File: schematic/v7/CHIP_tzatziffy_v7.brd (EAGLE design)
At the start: 40.9 x 49.8 mm, 56 parts, among them J1 2X20-CHIP0.7_DRILL, Q2 2N7002ET1G, U1 LMR62421, U3 DS2431P, X1 FH12-40S-0.5SH

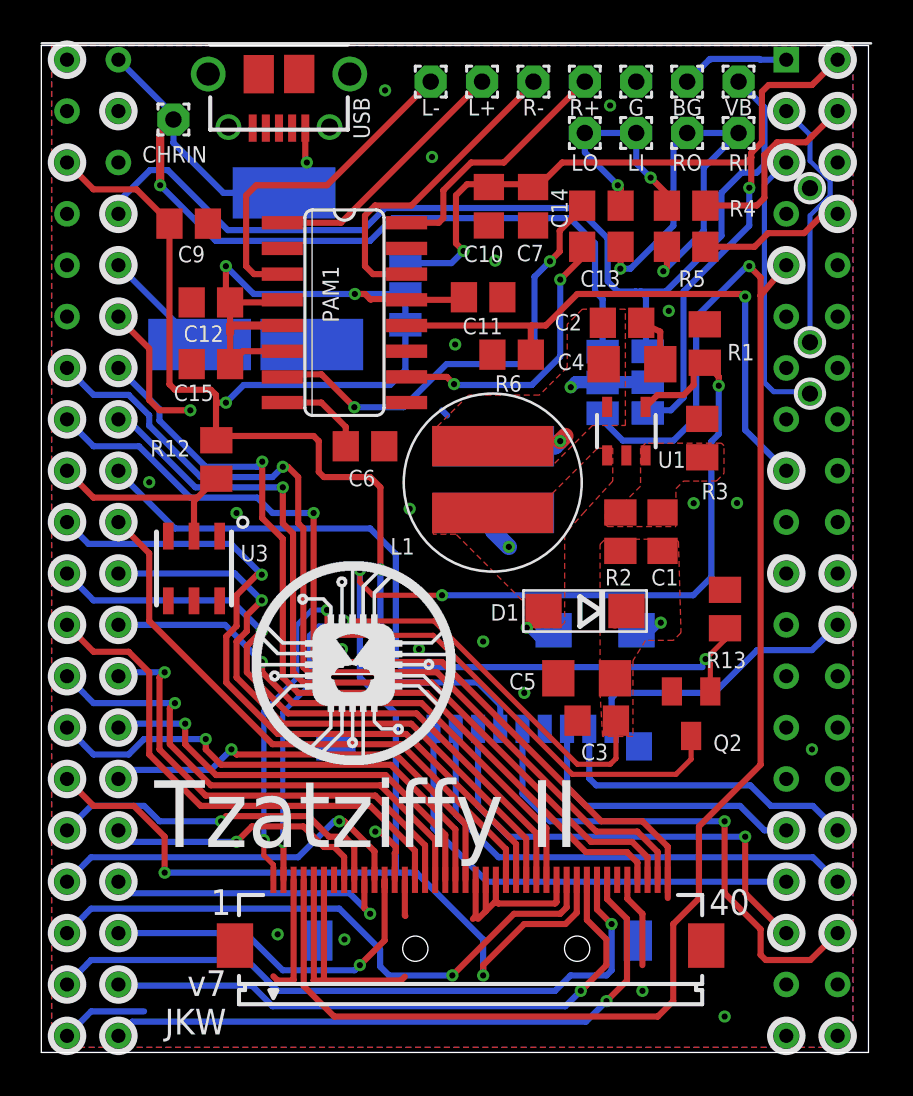
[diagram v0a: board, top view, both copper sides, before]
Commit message: added power supply
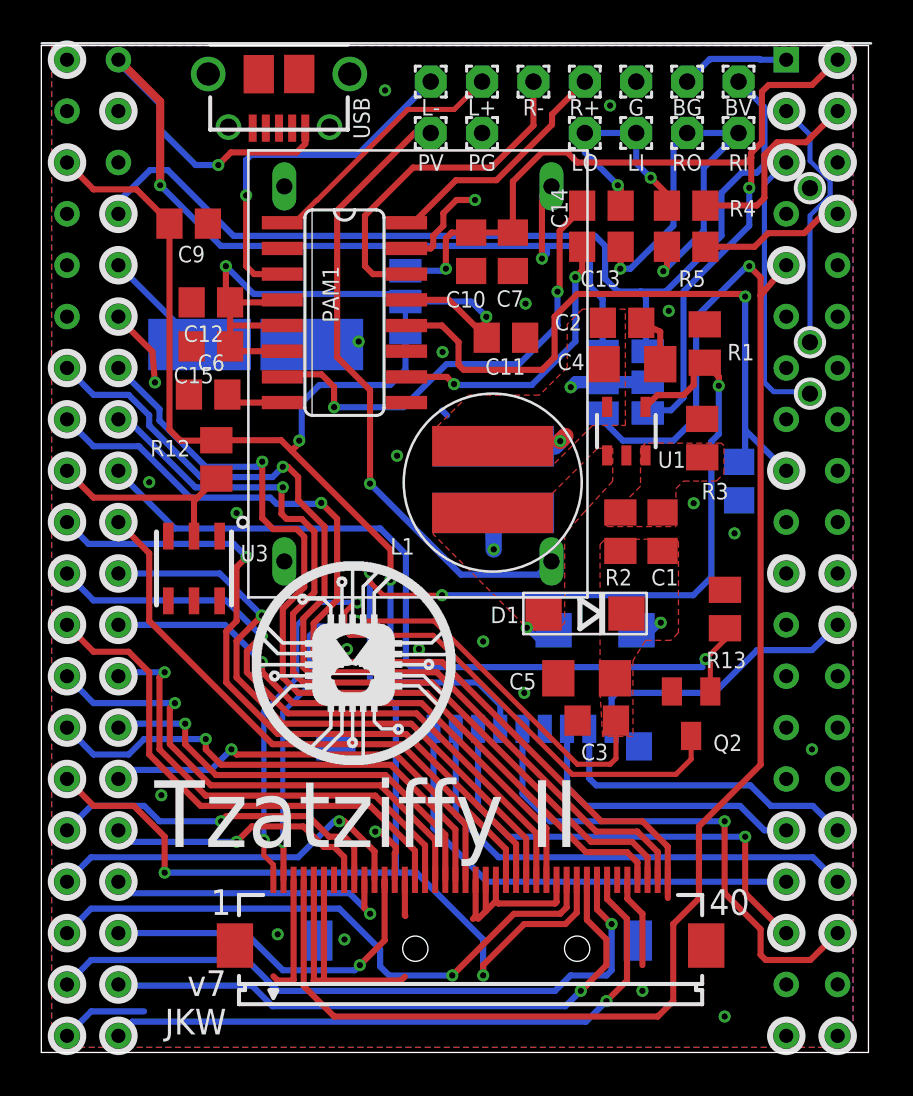
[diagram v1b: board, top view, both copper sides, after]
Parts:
- removed CHRIN: (no value), wirepad:1,6/0,8
- removed CHRIN_P: CHRIN, wirepad:SMD2,54-5,08
- added PG, PV: (no value), wirepad:1,6/0,8
- added U$10: MP1584EN, JKW_CHIP:MP1584EN
- SJ3, SJ4: value (none) -> SMD_SJ_3WAY_CLOSED; device SparkFun-Retired:SJ_2 -> JKW_CHIP:SMD_SJ_3WAY_CLOSED
- moved R6 12.9 mm to (34.5, 28.2), flipped to the bottom, turned to 90 degrees
- moved C6 8.16 mm to (8.25, 32.5), turned to 180 degrees
- moved C7 2.46 mm to (23.3, 39.6)
- moved C10 2.41 mm to (21.3, 39.6)
- moved C11 2.29 mm to (23.0, 35.3)
- moved C15 0.88 mm to (8.38, 34.9)
- moved SJ3 0.38 mm to (18.0, 37.1), turned to 90 degrees
- moved D1 0.12 mm to (26.9, 21.7)
- renumbered VB to BV
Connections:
- net N$26 renamed VCC3V3_2
- new net AMP_PWR: C11.2, C12.2, C15.1, PAM1.13, PAM1.4, PAM1.5, PAM1.6, SJ3.2
- new net DC_IN: C2.1, C4.1, L1.P$2, L2.P$2, SJ1.2, SJ4.2, U1.5
- new net PWR_IN: PV.1, U$10.VIN
- net GND: now also PG.1, U$10.GNDIN, U$10.GNDOUT
- net VCC3V3: now also SJ3.1; no longer C11.2, C12.2, C15.1, PAM1.13, PAM1.4, PAM1.5, PAM1.6, SJ3.2, SJ3.3
- net VCC5V: now also SJ3.3; no longer SJ3.1
- net VOUT: now also U$10.VOUT; no longer C2.1, C4.1, CHRIN.1, CHRIN_P.1, L1.P$2, L2.P$2, SJ1.2, SJ4.2, U1.5
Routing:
- net VCC3V3: track 89.3 -> 54.6 mm, vias 4 -> 2
- net AMP_PWR: track 0.00 -> 31.6 mm, vias 0 -> 2
- net PWR_IN: track 0.00 -> 31.5 mm, vias 0 -> 1
- net DC_IN: track 0.00 -> 8.02 mm, vias 0 -> 2
- net VOUT: track 57.6 -> 52.8 mm, vias 4 -> 3
- net GP3: track 28.4 -> 32.2 mm
- net GND: track 59.6 -> 61.5 mm, vias 23 -> 25
- net N$38: track 4.59 -> 2.88 mm
- net LCD_XR: track 42.8 -> 44.4 mm
- net LCD_YU: track 45.2 -> 46.7 mm
- net DISPL_GND: track 38.7 -> 40.2 mm
- net LCD_YD: track 41.3 -> 42.7 mm
- net N$35: track 15.8 -> 17.1 mm
- net VBAT_EXT: track 49.4 -> 48.2 mm
- net N$33: track 16.9 -> 17.9 mm, vias 0 -> 1
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- added copper zone on layer 1, net DC_IN
- removed copper zone on layer 1, net VOUT

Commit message: optimized routing
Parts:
- moved C13 4.95 mm to (32.2, 41.9), turned to 270 degrees
- moved R5 3.14 mm to (34.2, 41.9), turned to 270 degrees
- moved R4 2.89 mm to (29.0, 41.9), turned to 270 degrees
- moved C14 0.81 mm to (26.9, 41.9), turned to 270 degrees
- turned C10 to 90 degrees
- turned C7 to 90 degrees
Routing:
- net N$43: track 21.7 -> 7.91 mm, vias 2 -> 0
- net N$40: track 10.0 -> 16.6 mm
- net VOUT: track 52.8 -> 46.8 mm, vias 3 -> 2
- net VCC5V: track 45.9 -> 40.2 mm
- net N$39: track 14.8 -> 19.8 mm
- net N$41: track 11.1 -> 7.86 mm, vias 2 -> 0
- net VBAT_EXT: track 48.2 -> 45.2 mm
- net LCD_XR: track 44.4 -> 41.9 mm
- net LCD_YD: track 42.7 -> 40.4 mm
- net GND: track 61.5 -> 59.4 mm, vias 25 -> 26
- net LCD_XL: track 47.4 -> 45.6 mm
- net LCD_YU: track 46.7 -> 44.9 mm
- net N$37: track 7.22 -> 6.06 mm
- net N$36: track 23.0 -> 22.2 mm

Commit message: optimized routing and schematic
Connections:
- net N$1 renamed SDIO_DAT0
- net N$25 renamed SDIO_CMD
- net N$27 renamed SDIO_DAT1
- net N$28 renamed SDIO_DAT3
- net N$31 renamed SDIO_DAT2
- net N$37 renamed AUDIO_R
- net N$40 renamed AUDIO_L
- net N$44 renamed SDIO_CLK
- net N$45 renamed SDIO_CARD
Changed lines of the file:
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@@
 <wire x1="25.625" y1="38.938" x2="25.521" y2="38.834" width="0.3048" layer="1"/>
 </signal>
-<signal name="N$37">
+<signal name="AUDIO_R">
 <contactref element="R5" pad="2"/>
 <contactref element="J1" pad="HPR"/>
@@
 <wire x1="29.926" y1="38.75" x2="32.166" y2="40.99" width="0.3048" layer="1"/>
 </signal>
-<signal name="N$40">
+<signal name="AUDIO_L">
 <contactref element="R4" pad="2"/>
 <contactref element="J1" pad="HPL"/>
@@
 <wire x1="29.001" y1="41" x2="28.991" y2="40.99" width="0.3048" layer="1"/>
 </signal>
-<signal name="N$31">
+<signal name="SDIO_DAT2">
 <contactref element="J1" pad="CSID2"/>
 <contactref element="SDIO" pad="1"/>
@@
 <wire x1="22.038" y1="8.442" x2="19.39" y2="11.09" width="0.3048" layer="16"/>
 </signal>
-<signal name="N$1">
+<signal name="SDIO_DAT0">
 <contactref element="J1" pad="CSID0"/>
 <contactref element="SDIO" pad="7"/>
@@
 <wire x1="35.754" y1="10.982" x2="36.83" y2="10.982" width="0.3048" layer="16"/>
 </signal>
-<signal name="N$25">
+<signal name="SDIO_CMD">
 <contactref element="J1" pad="CSID4"/>
 <contactref element="SDIO" pad="3"/>
@@
 <wire x1="36.77" y1="5.902" x2="36.83" y2="5.902" width="0.3048" layer="1"/>
 </signal>
-<signal name="N$27">
+<signal name="SDIO_DAT1">
 <contactref element="SDIO" pad="8"/>
 <contactref element="J1" pad="CSID1"/>
@@
 <wire x1="38.14" y1="12.192" x2="39.37" y2="10.982" width="0.3048" layer="16"/>
 </signal>
-<signal name="N$28">
+<signal name="SDIO_DAT3">
 <contactref element="J1" pad="CSID3"/>
 <contactref element="SDIO" pad="2"/>
@@
 <wire x1="38.14" y1="9.652" x2="39.37" y2="8.442" width="0.3048" layer="16"/>
 </signal>
-<signal name="N$44">
+<signal name="SDIO_CLK">
 <contactref element="SDIO" pad="5"/>
 <contactref element="J1" pad="CSID5"/>
@@
 <wire x1="33.782" y1="7.874" x2="33.782" y2="11.43" width="0.3048" layer="1"/>
 </signal>
-<signal name="N$45">
+<signal name="SDIO_CARD">
 <contactref element="J1" pad="AP-EINT3"/>
 <contactref element="SDIO" pad="9"/>

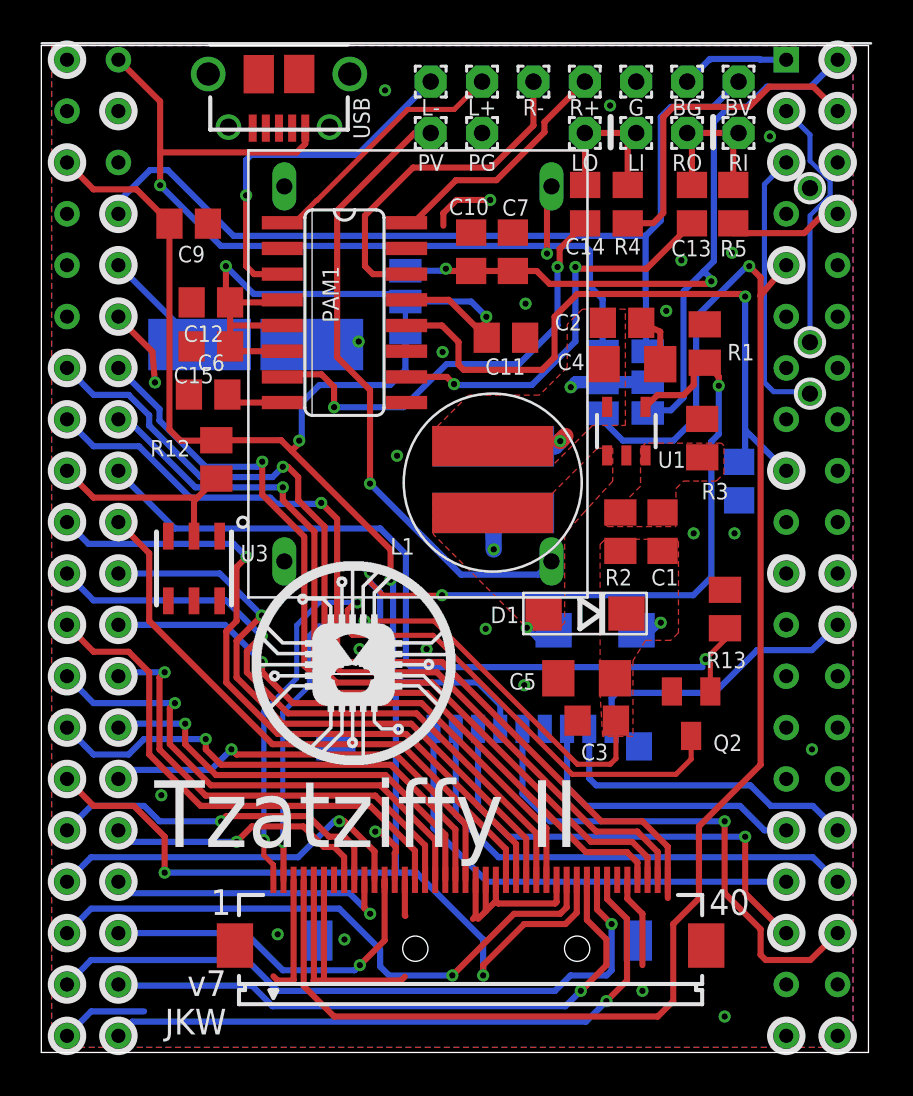
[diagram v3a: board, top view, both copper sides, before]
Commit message: improved routing
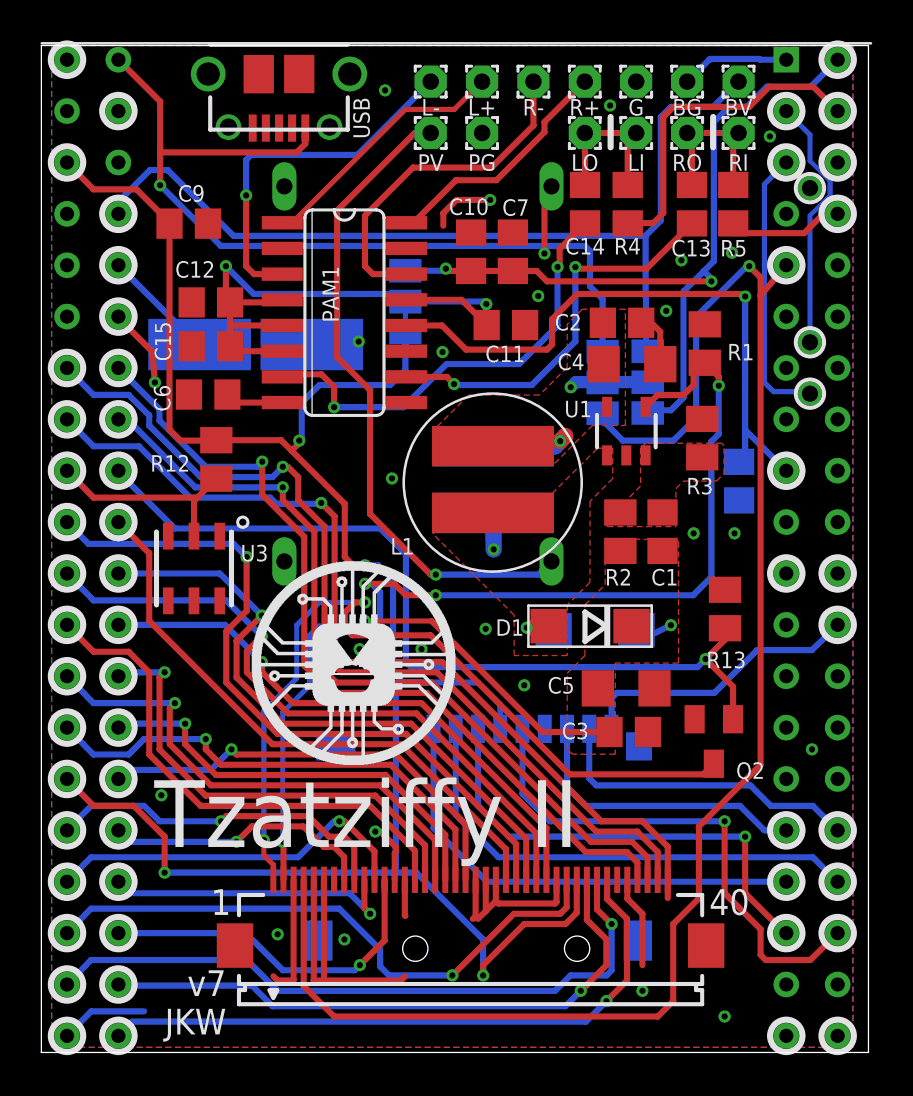
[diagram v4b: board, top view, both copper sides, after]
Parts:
- U$10: value MP1584EN -> MP1584EN_FRAMELESS; device JKW_CHIP:MP1584EN -> JKW_CHIP:MP1584EN_FRAMELESS
- moved C5 2.02 mm to (28.9, 18.0), turned to 0 degrees
- moved Q2 1.78 mm to (33.2, 15.4)
- moved C3 1.68 mm to (29.0, 15.8), turned to 0 degrees
- moved D1 0.67 mm to (27.1, 21.1)
- moved C11 0.62 mm to (23.0, 36.0)
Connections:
- net N$32 renamed L+OUT
- net N$33 renamed L-OUT
- net N$34 renamed R+OUT
- net N$35 renamed R-OUT
- net N$36 renamed INL
- net N$39 renamed INR
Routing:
- net PWR_LGT: track 36.7 -> 32.0 mm
- net GP3: track 32.2 -> 30.3 mm
- net PWM: track 40.2 -> 42.1 mm
- net PWR_IN: track 31.5 -> 32.4 mm
- net DISPL_GND: track 40.0 -> 40.7 mm
- net VCC3V3: track 54.5 -> 55.3 mm
- net VREG_OUTPUT: track 4.50 -> 3.77 mm
- net L+OUT: track 12.8 -> 13.4 mm
- net AMP_PWR: track 31.6 -> 32.2 mm
- net EN: track 83.1 -> 82.5 mm

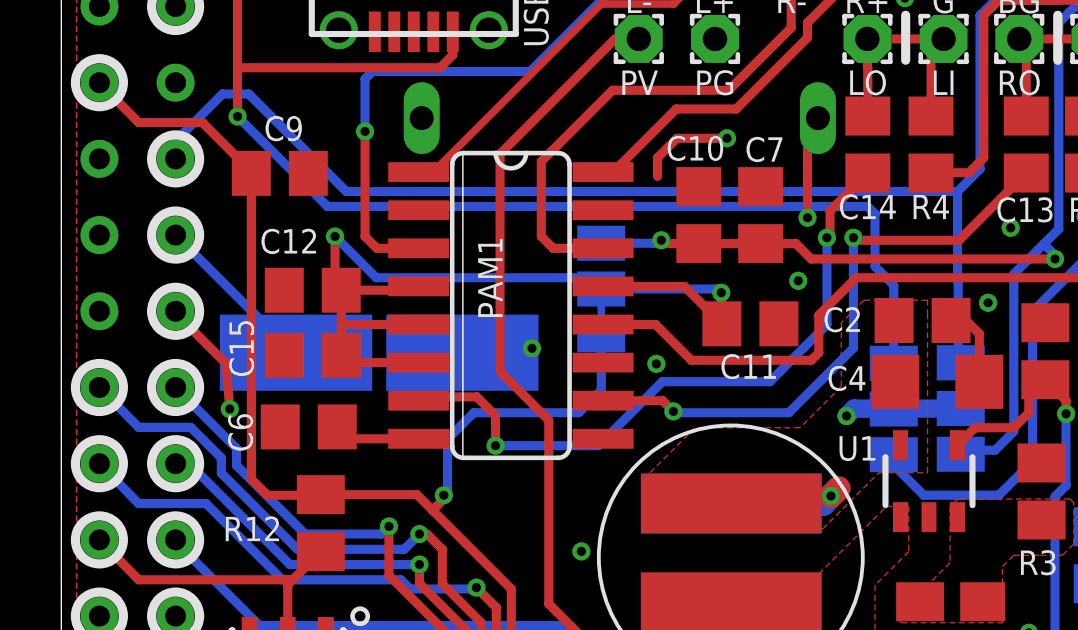
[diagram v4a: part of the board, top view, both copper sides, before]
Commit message: improved routing
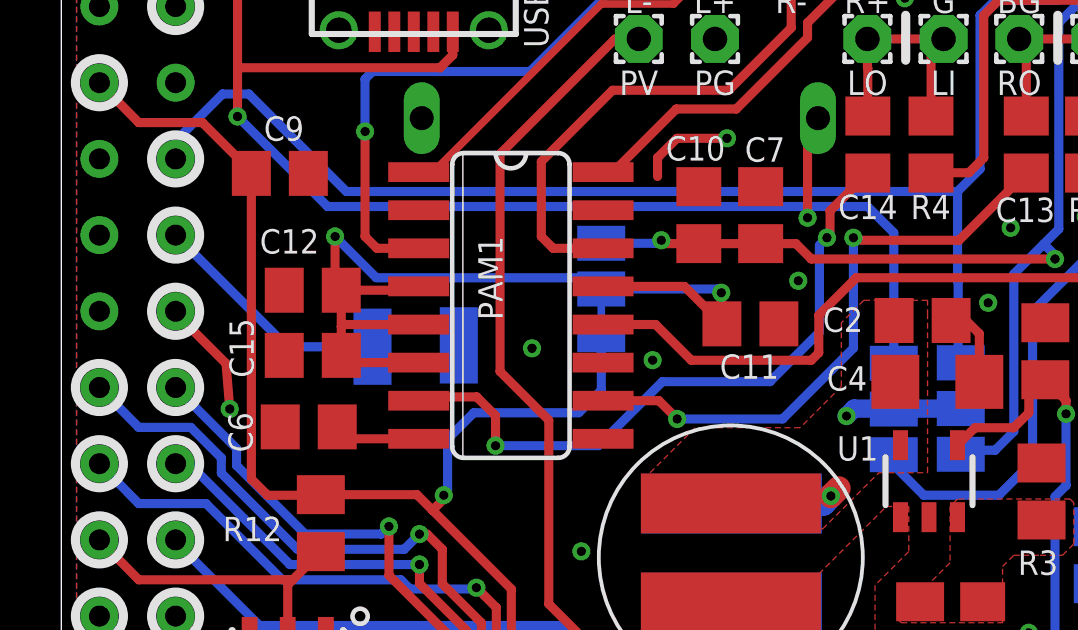
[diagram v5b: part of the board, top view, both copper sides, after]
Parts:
- BTN, GND: device wirepad:SMD2,54-5,08 -> wirepad:SMD1,27-2,54
- moved BTN 2.56 mm to (10.4, 35.2), turned to 180 degrees
- moved U$5 1.53 mm to (5.10, 22.1)
- moved GND 0.27 mm to (13.2, 35.2), turned to 180 degrees
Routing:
- net PWR_ON: track 7.21 -> 8.11 mm
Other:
- board text removed: "CHRIN"
